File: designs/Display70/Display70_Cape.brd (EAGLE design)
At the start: 200.7 x 121.9 mm, 36 parts, among them IC13 FAN5333BSX

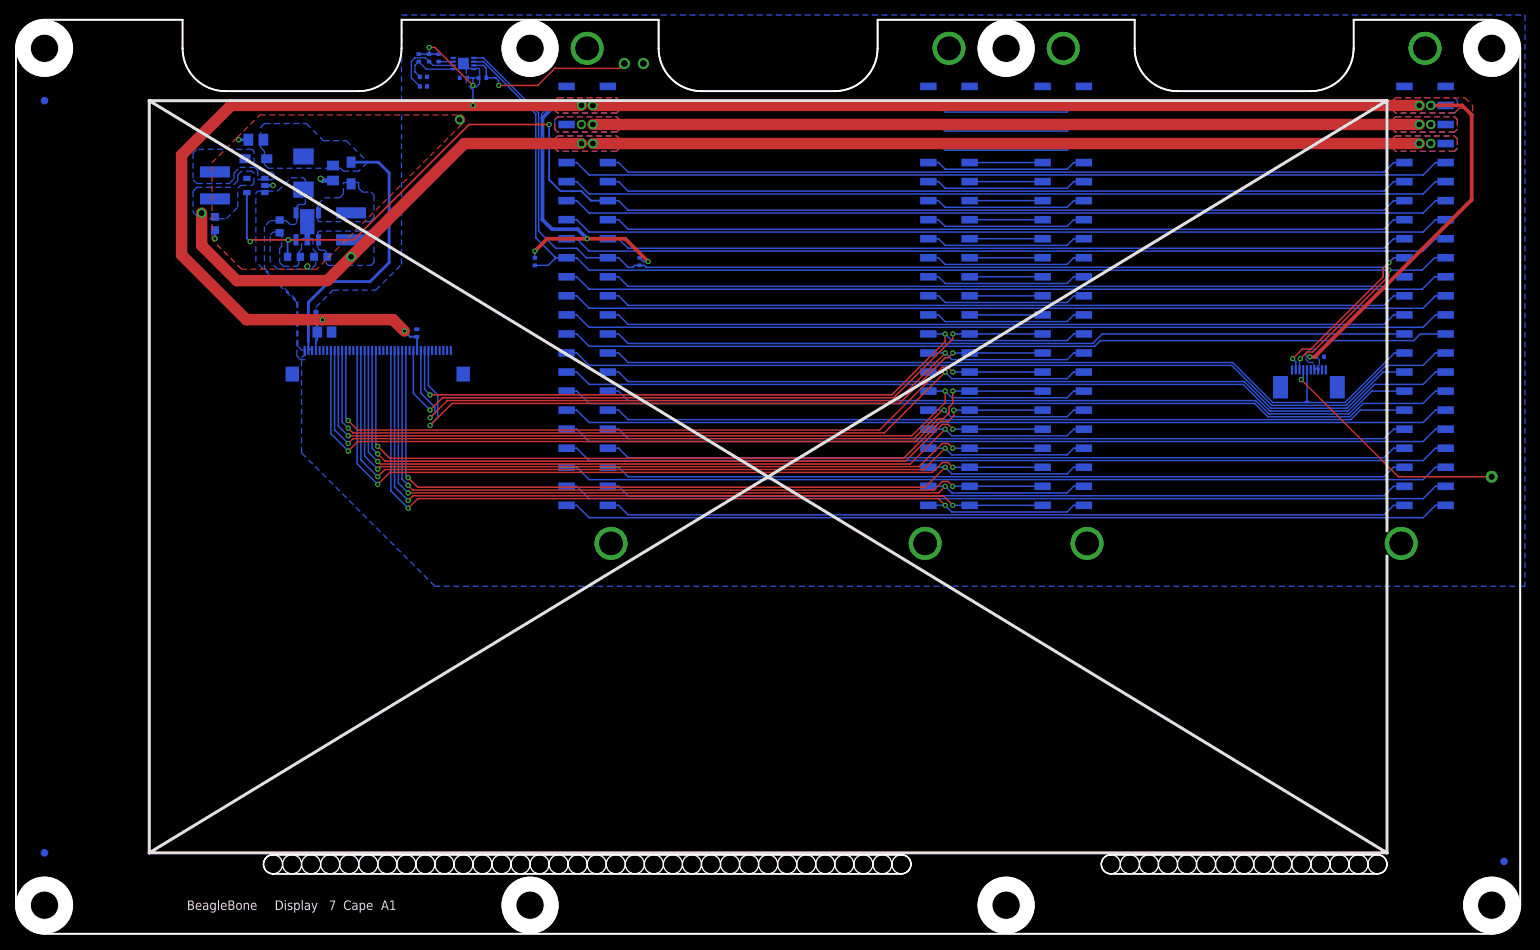
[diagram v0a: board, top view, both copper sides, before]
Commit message: Added the revised EAGLE schematics. Also removed two files that were probably not intended to be added as they are lock files in EAGLE.
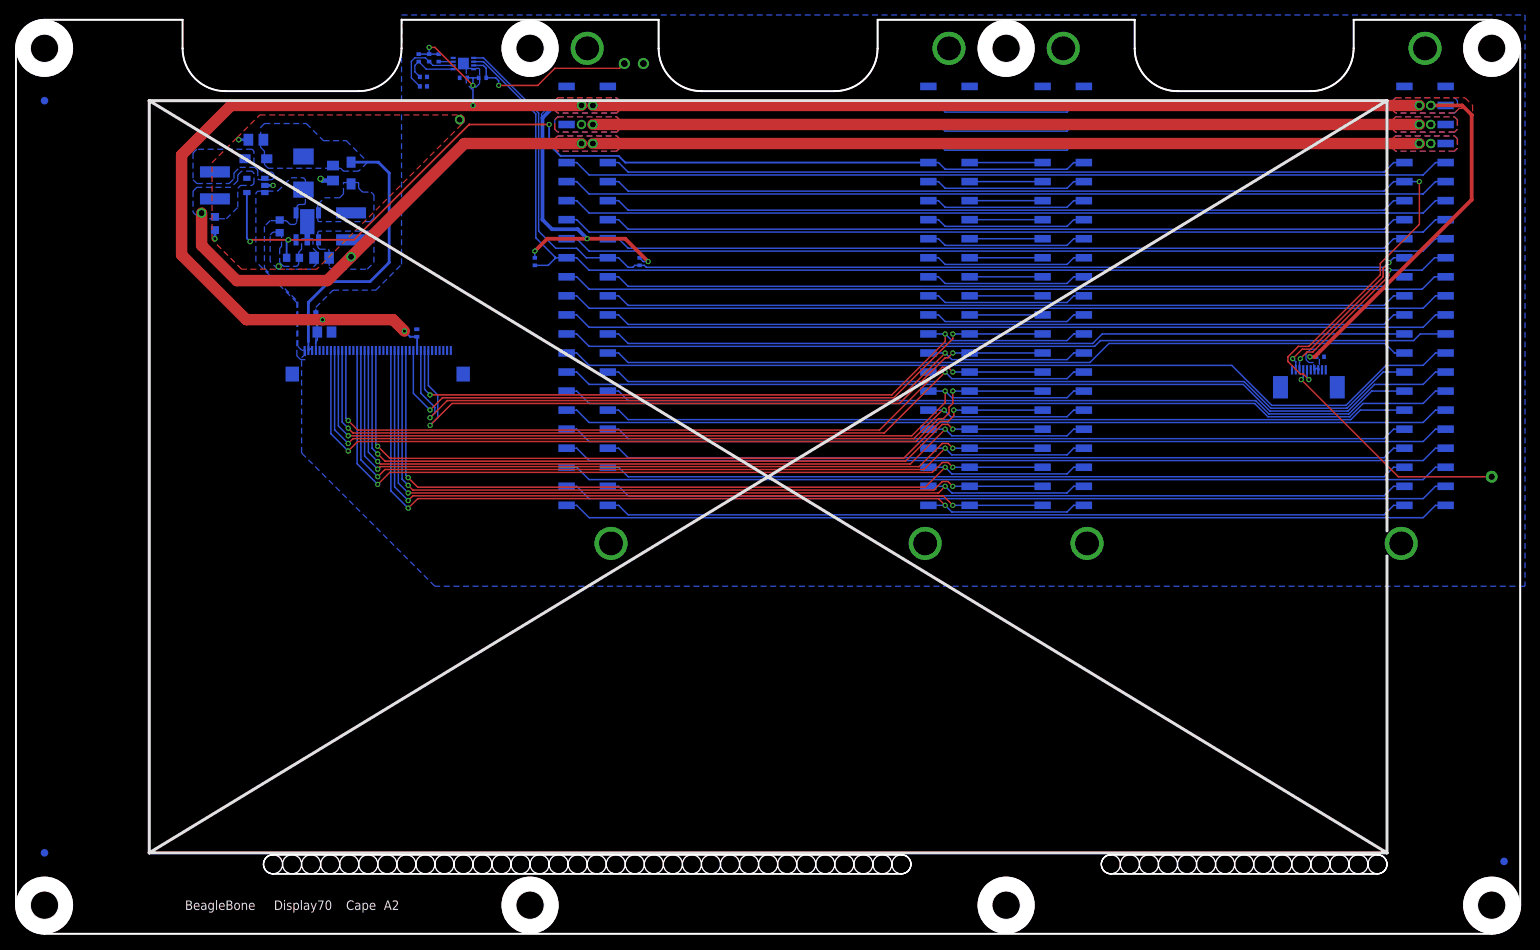
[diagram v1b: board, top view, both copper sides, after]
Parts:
- C5: device rcl:C0603K -> rcl:C0805K
- moved C5 0.18 mm to (40.8, 90.2)
- moved R1 0.18 mm to (37.0, 90.2)
- renumbered X3 to X1
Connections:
- removed net P8.9: BB.DISPLAY.CAPE-(BEAGLEBONE).B8.9, BB.DISPLAY.CAPE-(CAPE).B8.9
- removed net P9.12: BB.DISPLAY.CAPE-(BEAGLEBONE).B9.12, BB.DISPLAY.CAPE-(CAPE).B9.12
- new net P9.14: BB.DISPLAY.CAPE-(BEAGLEBONE).B9.14, BB.DISPLAY.CAPE-(CAPE).B9.14
- new net P9.30: BB.DISPLAY.CAPE-(BEAGLEBONE).B9.30, BB.DISPLAY.CAPE-(CAPE).B9.30
- net CAP.TOUCH.IRQ: now also BB.DISPLAY.CAPE-(BEAGLEBONE).B9.12, BB.DISPLAY.CAPE-(CAPE).B9.12; no longer BB.DISPLAY.CAPE-(BEAGLEBONE).B9.30, BB.DISPLAY.CAPE-(CAPE).B9.30
- net LCD.BACKLIGHT: now also BB.DISPLAY.CAPE-(BEAGLEBONE).B8.9, BB.DISPLAY.CAPE-(CAPE).B8.9; no longer BB.DISPLAY.CAPE-(BEAGLEBONE).B9.14, BB.DISPLAY.CAPE-(CAPE).B9.14
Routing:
- net P9.30: track 0.00 -> 108.4 mm
- net P9.14: track 0.00 -> 107.3 mm
- net P9.12: track 107.3 -> 0.00 mm
- net LCD.BACKLIGHT: track 180.1 -> 132.3 mm
- net CAP.TOUCH.IRQ: track 116.8 -> 146.6 mm, vias 0 -> 2
- net P8.9: track 21.5 -> 0.00 mm
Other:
- board text added: "A2"
- board text added: "Display70"
- board text removed: "7"
- board text removed: "Display"
